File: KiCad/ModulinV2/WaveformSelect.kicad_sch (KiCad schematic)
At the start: 22 parts, among them IC10 SN74AHCT1G00DBVR, IC11 SN74AHCT1G00DBVR, IC12 SN74AHC1G08DBVR, IC13 SN74AHC1G02DBVR, IC14 SN74AHCT1G00DBVR, IC15 SN74AHC1G02DBVR, IC16 SN74HC193DR, IC17 TMUX4052DYYR, IC18 TMUX4051DYYRQ1, IC19 TMUX4051DYYRQ1, IC9 NC7SZ74K8X

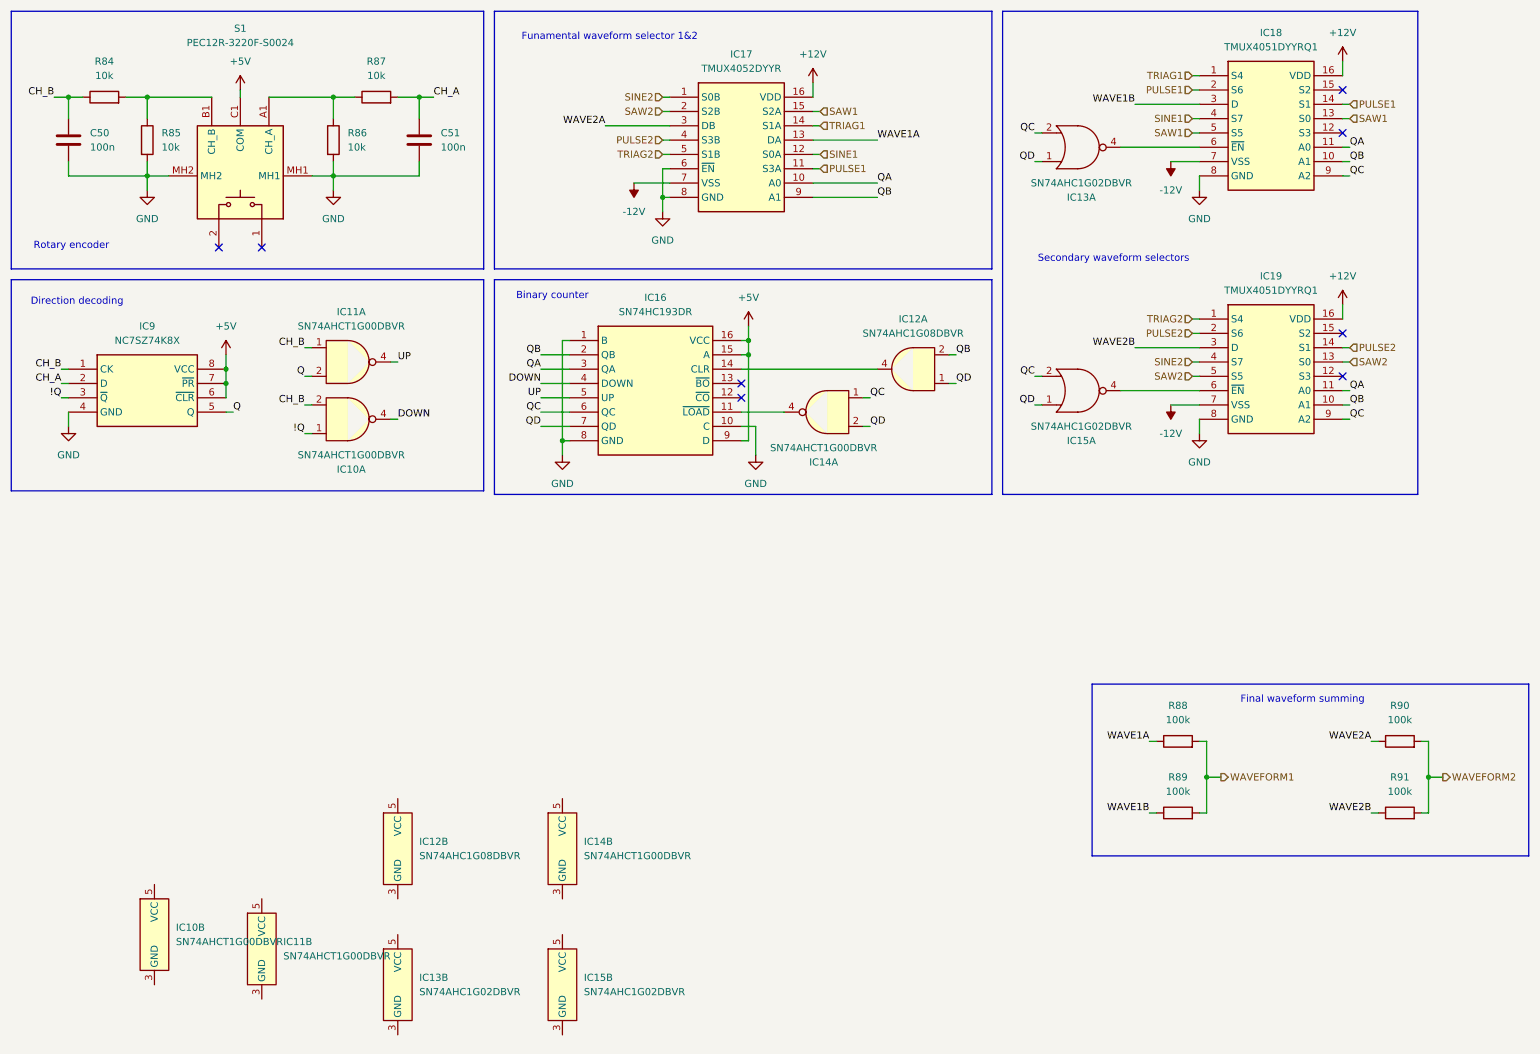
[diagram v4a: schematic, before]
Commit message: Designed ADSR and better tuning schematics with digital/manual capability
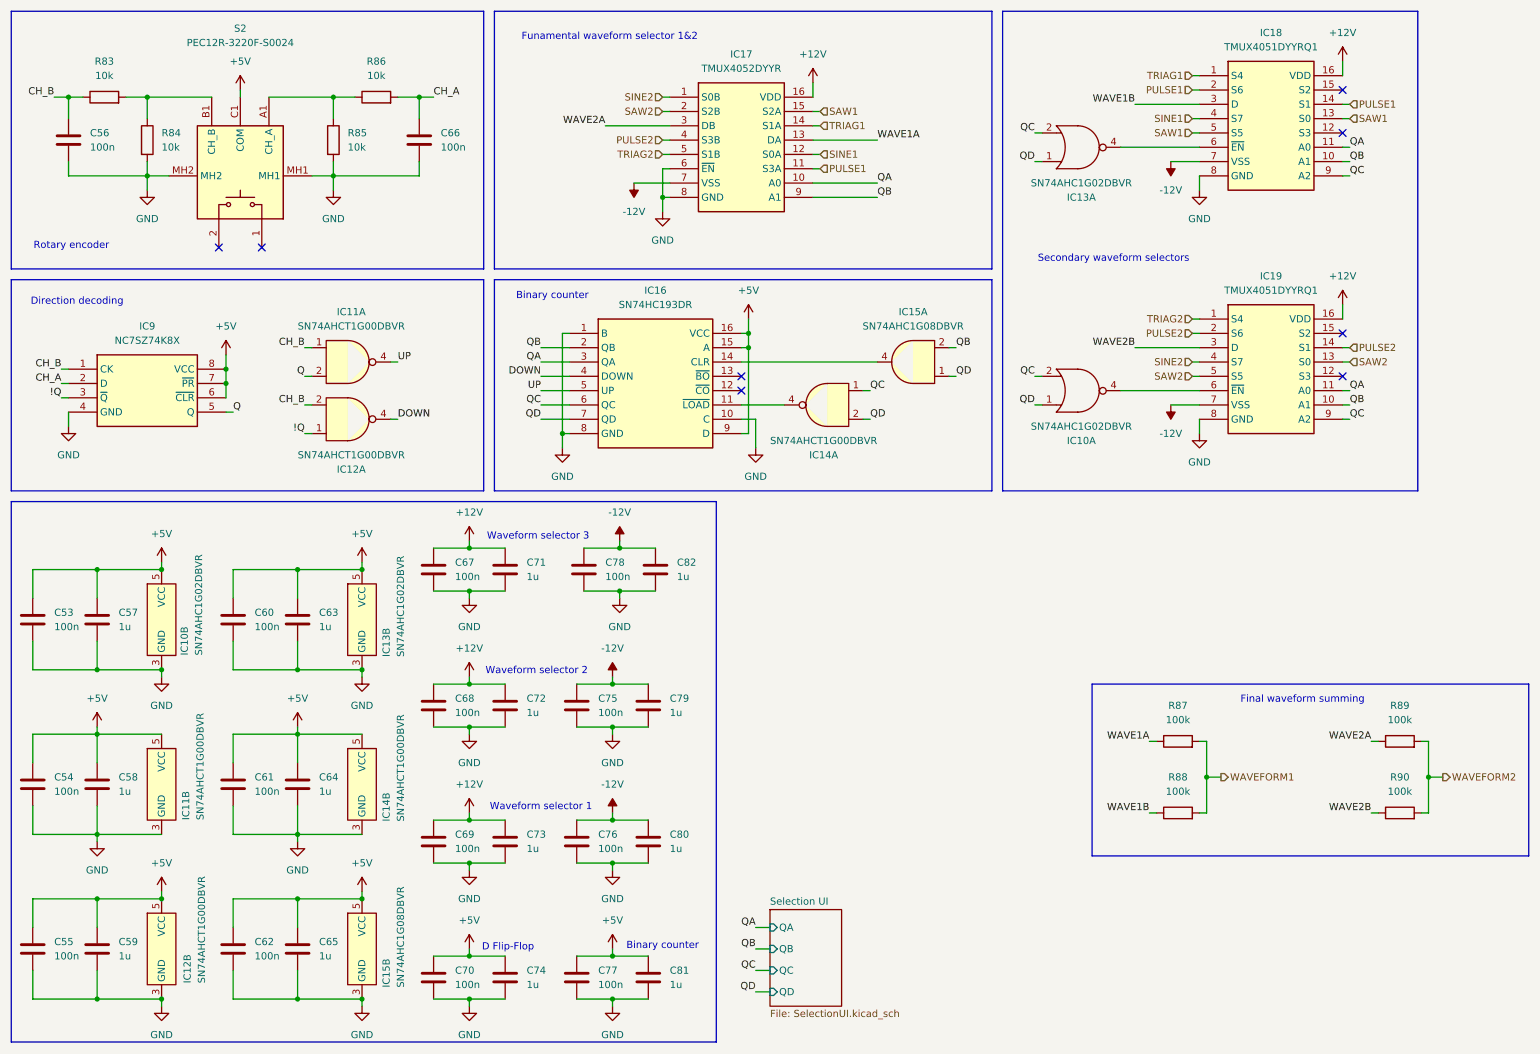
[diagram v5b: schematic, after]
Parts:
- added C53, C54, C55, C60, C61, C62, C67, C68, C69, C70, C75, C76, C77, C78: 100n, symbol Device:C
- added C57, C58, C59, C63, C64, C65, C71, C72, C73, C74, C79, C80, C81, C82: 1u, symbol Device:C
- renumbered C50 to C56, C51 to C66, IC15 to IC10, IC10 to IC12, IC12 to IC15, R84 to R83, R85 to R84, R86 to R85, R87 to R86, R88 to R87, R89 to R88, R90 to R89, R91 to R90, S1 to S2
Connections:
- net +12V: now also C67.2, C68.2, C69.2, C71.2, C72.2, C73.2
- net +5V: now also IC10.5 (VCC), IC11.5 (VCC), IC12.5 (VCC), IC13.5 (VCC), IC14.5 (VCC), IC15.5 (VCC), C53.2, C54.2, C55.2, C57.2, C58.2, C59.2, C60.2, C61.2, C62.2, C63.2, C64.2, C65.2, C70.2, C74.2, C77.2, C81.2
- net -12V: now also C75.2, C76.2, C78.2, C79.2, C80.2, C82.2
- net GND: now also IC10.3 (GND), IC11.3 (GND), IC12.3 (GND), IC13.3 (GND), IC14.3 (GND), IC15.3 (GND), C53.1, C54.1, C55.1, C57.1, C58.1, C59.1, C60.1, C61.1, C62.1, C63.1, C64.1, C65.1, C67.1, C68.1, C69.1, C70.1, C71.1, C72.1, C73.1, C74.1, C75.1, C76.1, C77.1, C78.1, C79.1, C80.1, C81.1, C82.1
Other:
- added sheet Selection UI (SelectionUI.kicad_sch)
- note added: "D Flip-Flop"
- note added: "Waveform selector 1"
- note added: "Waveform selector 2"
- note added: "Waveform selector 3"
- moved on the sheet: IC10B, IC11B, IC12B, IC13B, IC14A, IC14B, IC15A, IC15B, IC16

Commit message: Added 4k7 pullups to I2C lines
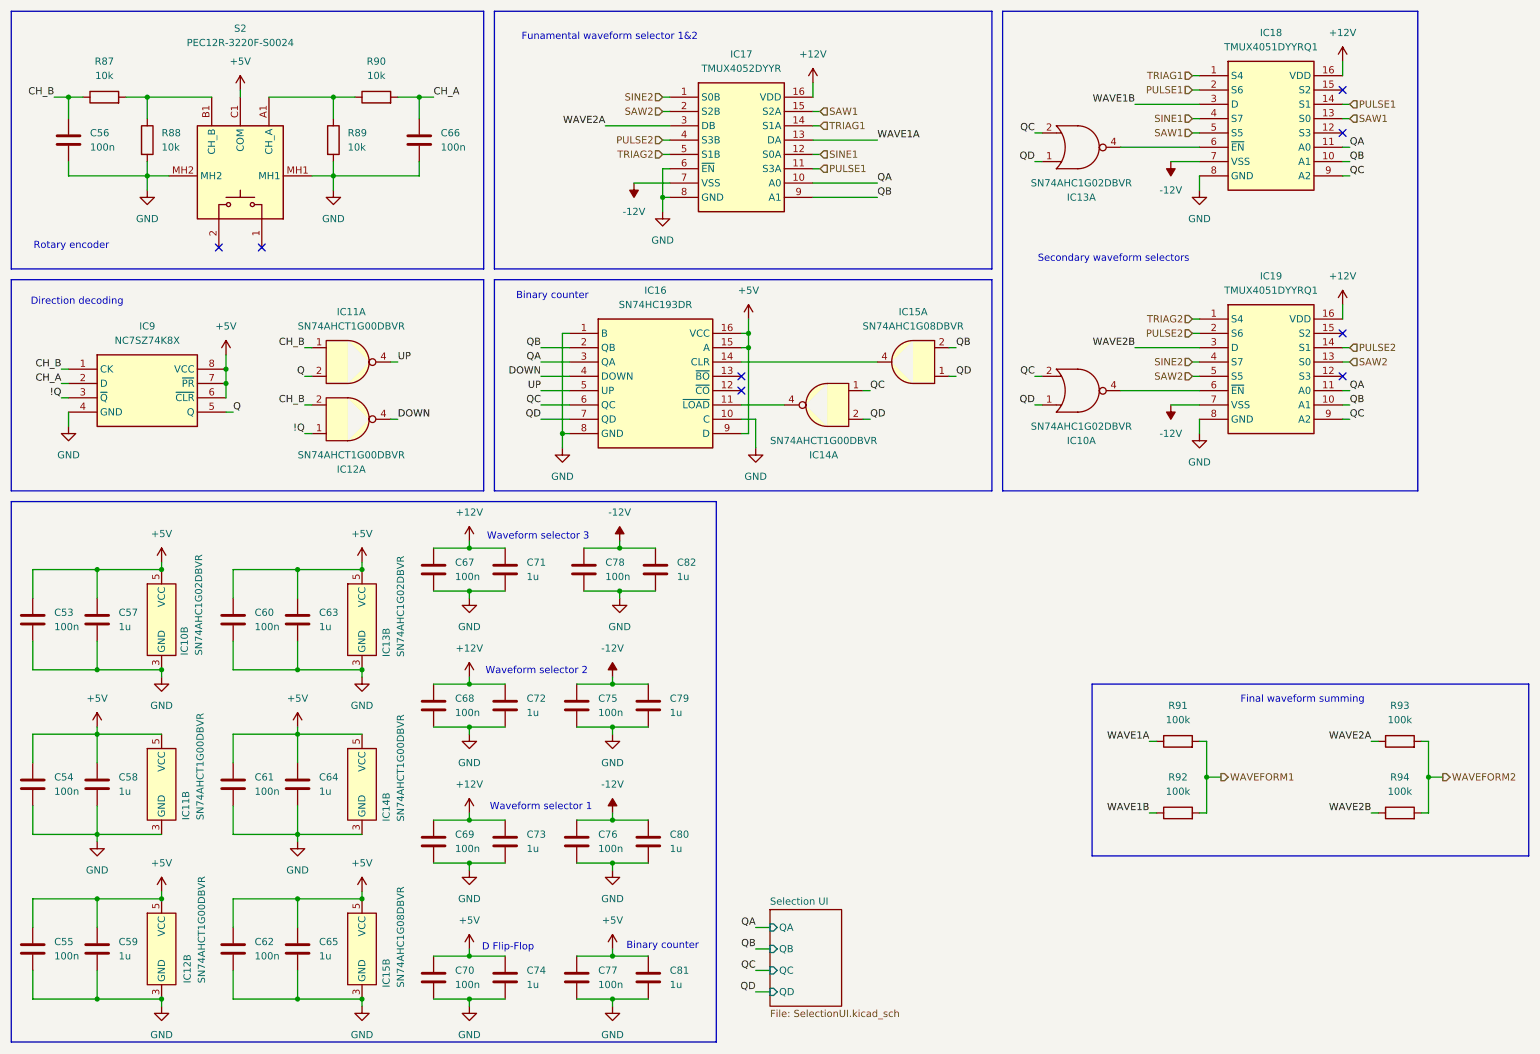
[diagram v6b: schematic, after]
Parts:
- renumbered R83 to R87, R84 to R88, R85 to R89, R86 to R90, R87 to R91, R88 to R92, R89 to R93, R90 to R94

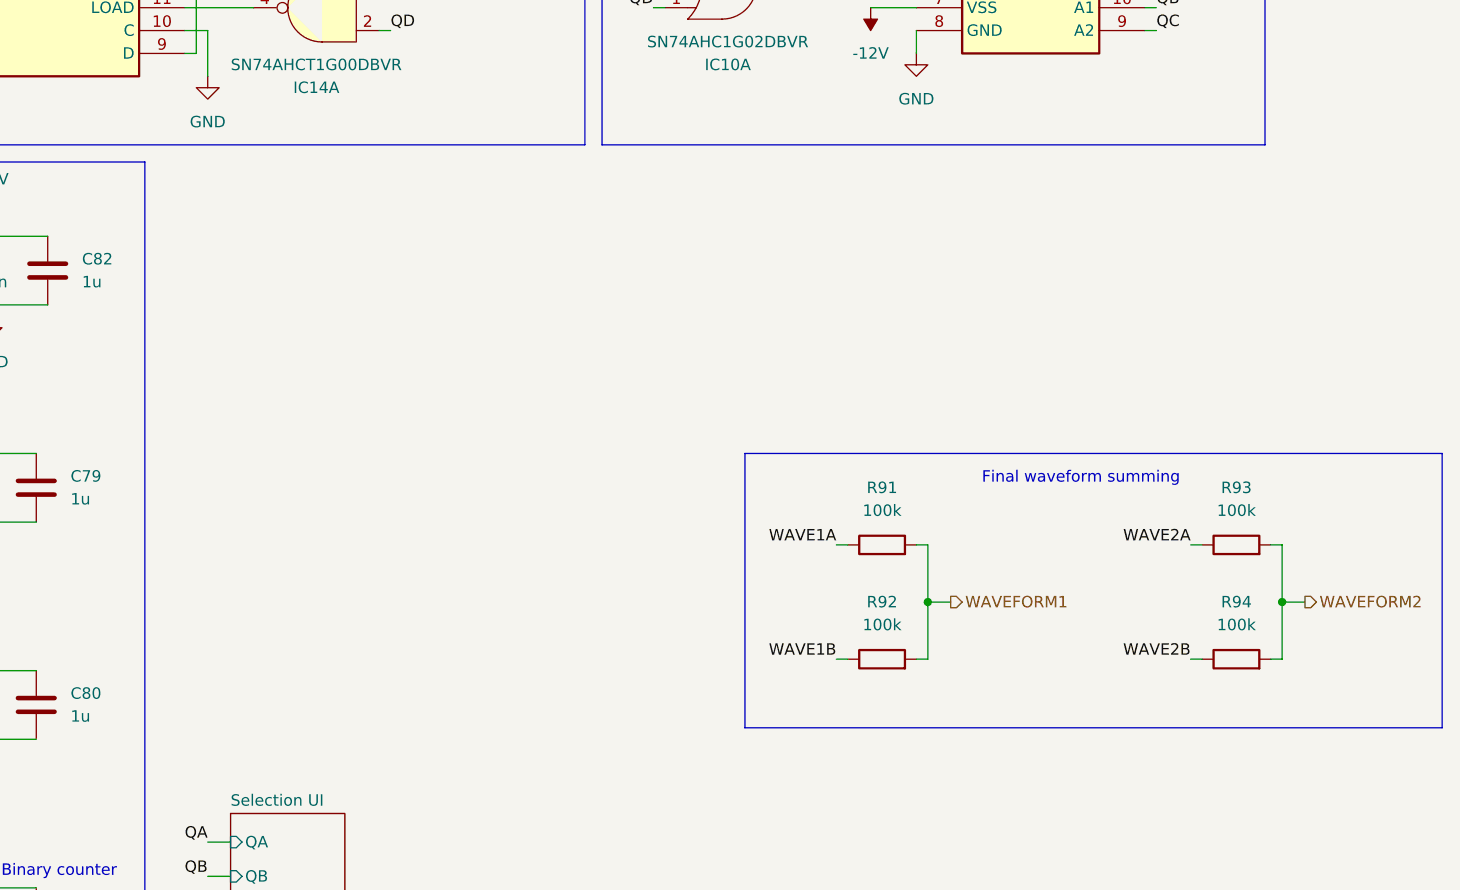
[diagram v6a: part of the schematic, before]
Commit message: Added wave selection jumpers for testing
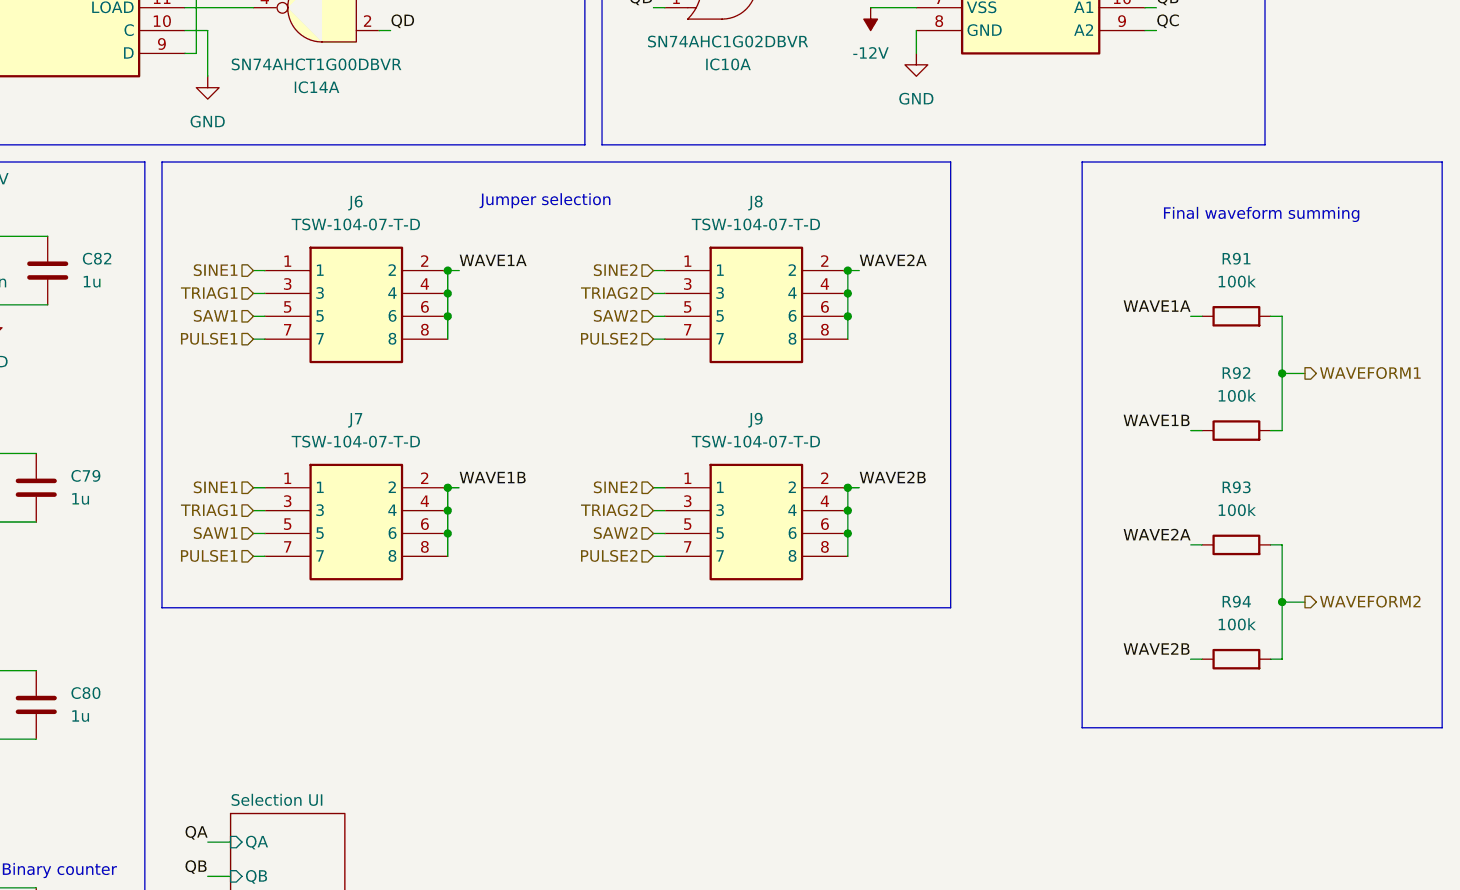
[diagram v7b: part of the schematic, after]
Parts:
- added J6, J7, J8, J9: TSW-104-07-T-D, TSW-104-XX-YY-D, symbol TSW-104-07-T-D:TSW-104-07-T-D
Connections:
- net PULSE1: now also J6.7, J7.7
- net PULSE2: now also J8.7, J9.7
- net SAW1: now also J6.5, J7.5
- net SAW2: now also J8.5, J9.5
- net SINE1: now also J6.1, J7.1
- net SINE2: now also J8.1, J9.1
- net TRIAG1: now also J6.3, J7.3
- net TRIAG2: now also J8.3, J9.3
- net WAVE1A: now also J6.2, J6.4, J6.6, J6.8
- net WAVE1B: now also J7.2, J7.4, J7.6, J7.8
- net WAVE2A: now also J8.2, J8.4, J8.6, J8.8
- net WAVE2B: now also J9.2, J9.4, J9.6, J9.8
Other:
- note added: "Jumper selection"
- moved on the sheet: R91, R92
